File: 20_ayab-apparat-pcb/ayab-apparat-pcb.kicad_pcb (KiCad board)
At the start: 2 copper layers, 105.9 x 43.2 mm, 61 parts, among them K1 CONN_3, K2 CONN_3, P10 CONN_2, P2 CONN_10, P3 CONN_10, P4 CONN_8, P5 CONN_5, P6 CONN_5, P7 CONN_3X2, P8 CONN_4, P9 CONN_2, Q1 MOSFET_P, SW1 SW_PUSH, U1 LM1117, U2 PCF8574, U3 PCF8574, U4 ULN2803, U5 ULN2803, U6 ATMEGA32U4-A, X1 16MHz, X2 USBMINI

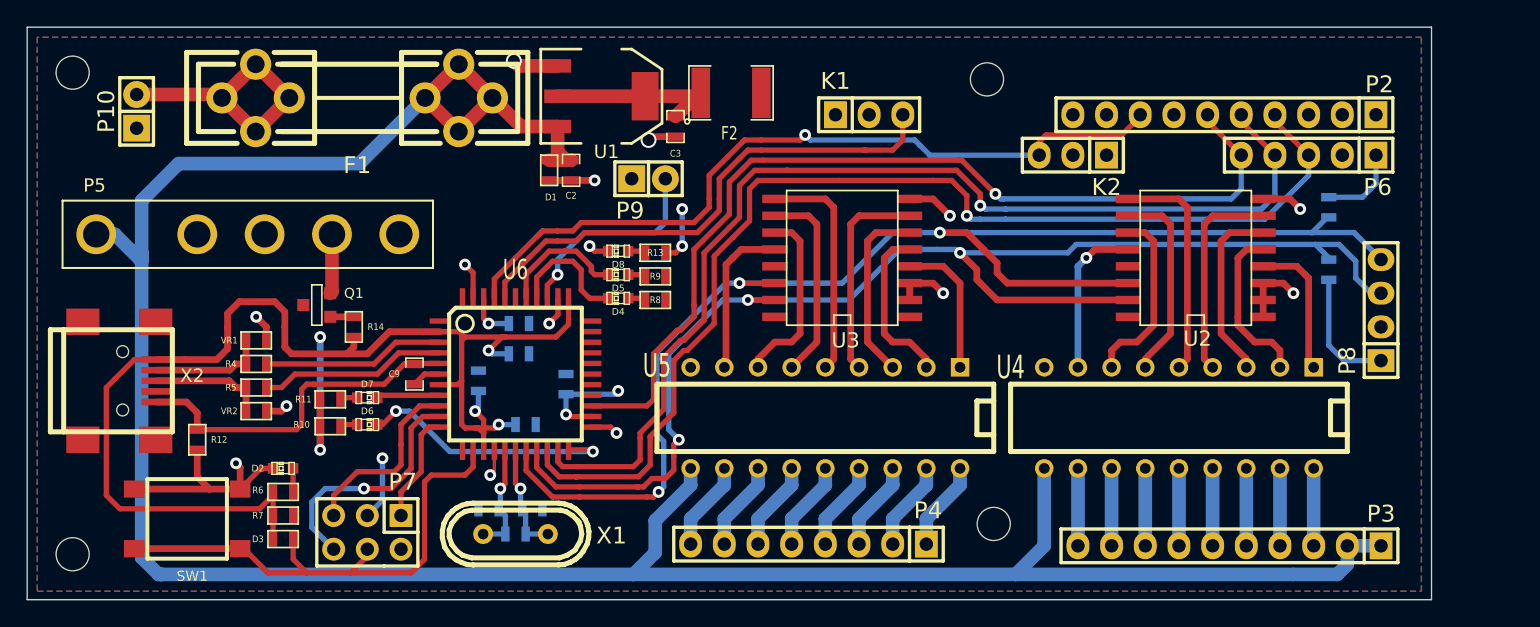
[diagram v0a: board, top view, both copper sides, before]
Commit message: chaned board size
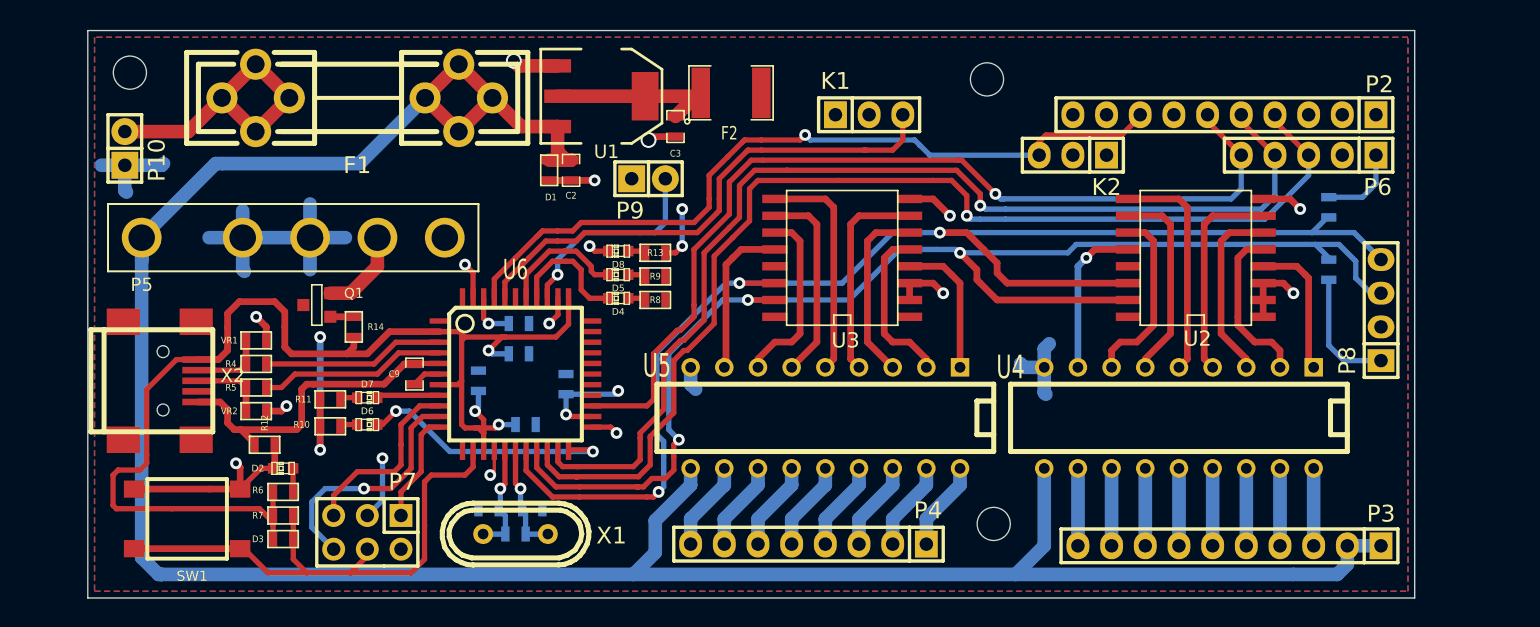
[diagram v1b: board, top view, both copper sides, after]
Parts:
- removed the MH at (62.1, 123.1)
- moved R12 5.09 mm to (76.6, 114.8), turned to 0 degrees
- moved MH 4.32 mm to (66.4, 86.7)
- moved P5 3.44 mm to (67.3, 99.2)
- moved X2 3.05 mm to (68.1, 110.0)
- moved P10 2.93 mm to (66.0, 92.5)
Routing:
- net GND: track 56.0 -> 89.2 mm
- net +12V: track 196.3 -> 188.6 mm
- net /atmega/D-: track 8.68 -> 5.64 mm
- net /atmega/D+: track 8.70 -> 5.65 mm
- net +5V_MACHINE: track 4.50 -> 6.56 mm
- net Net-(F1-Pad2): track 20.9 -> 22.7 mm
- net /atmega/RESET: track 39.6 -> 41.4 mm
- net /atmega/UGND: track 26.6 -> 24.9 mm
- net VUSB: track 94.0 -> 92.9 mm
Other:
- board size 105.9 x 43.2 mm -> 100.1 x 42.8 mm

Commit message: final version (ordered)
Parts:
- moved K1 2.54 mm to (122.2, 87.4)
- moved P2 2.41 mm to (149.0, 87.5)
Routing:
- net /atmega/EOL_L: track 39.0 -> 41.7 mm
- net /atmega/V1: track 81.7 -> 84.1 mm
- net /atmega/BELTSHIFT: track 71.3 -> 73.7 mm
- net /atmega/V2: track 85.4 -> 87.8 mm
- net /atmega/EOL_R: track 58.6 -> 61.1 mm
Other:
- board text added: "ayab-knitting.com"
- board text removed: "thinkstack (c) 2014"
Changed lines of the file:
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@@
     (links 180)
     (no_connects 1)
-    (area 36.46823 73.617524 164.856886 139.0142)
+    (area 40.78623 73.617524 164.856886 133.1341)
     (thickness 1.6)
     (drawings 7)
-    (tracks 708)
+    (tracks 713)
     (zones 0)
     (modules 60)
@@
   )
   (setup
-    (last_trace_width 1.027)
+    (last_trace_width 0.4)
     (user_trace_width 0.4)
     (user_trace_width 0.508)
@@
     (visible_elements FFFFFF7F)
     (pcbplotparams
-      (layerselection 3178497)
+      (layerselection 284196865)
       (usegerberextensions true)
       (excludeedgelayer true)
@@
       (outputformat 1)
       (mirror false)
-      (drillshape 1)
+      (drillshape 0)
       (scaleselection 1)
-      (outputdirectory ""))
+      (outputdirectory out/))
   )
   (net 0 "")
@@
     (tags "LED led 0603 SMD smd SMT smt smdled SMDLED smtled SMTLED")
     (attr smd)
-    (fp_text reference D4 (at 0 -1.016 180) (layer F.SilkS)
+    (fp_text reference D4 (at 0 -0.889 180) (layer F.SilkS)
       (effects (font (size 0.508 0.508) (thickness 0.127)))
     )
@@
     (tags "LED led 0603 SMD smd SMT smt smdled SMDLED smtled SMTLED")
     (attr smd)
-    (fp_text reference D5 (at 0 -1.016 180) (layer F.SilkS)
+    (fp_text reference D5 (at 0 -0.889 180) (layer F.SilkS)
       (effects (font (size 0.508 0.508) (thickness 0.127)))
     )
@@
     (tags "LED led 0603 SMD smd SMT smt smdled SMDLED smtled SMTLED")
     (attr smd)
-    (fp_text reference D8 (at 0 -1.016 180) (layer F.SilkS)
+    (fp_text reference D8 (at 0 -0.889 180) (layer F.SilkS)
       (effects (font (size 0.508 0.508) (thickness 0.127)))
     )
@@
     (descr "Fuseholder, 5x20, open, horizontal, Type-III, universal, inline, lateral,")
     (tags "Fuseholder, 5x20, open, horizontal, Type-III, universal, inline, lateral, Sicherungshalter, offen,")
-    (fp_text reference F1 (at 0 -5.08 180) (layer F.SilkS)
+    (fp_text reference F1 (at -11.684 -4.826 180) (layer F.SilkS)
       (effects (font (thickness 0.3048)))
     )
@@
   )
   (module Pin_Headers:Pin_Header_Straight_1x03 (layer F.Cu)
-    (at 122.174 89.916)
+    (at 122.174 87.376)
     (descr "1 pin")
     (tags "CONN DEV")
@@
   )
   (module Pin_Headers:Pin_Header_Straight_1x10 (layer F.Cu)
-    (at 148.971 89.916 180)
+    (at 148.971 87.503 180)
     (descr "1 pin")
     (tags "CONN DEV")
@@
     (descr "USB Mini-B 5-pin SMD connector")
     (tags "USB, Mini-B, connector")
-    (fp_text reference X2 (at 6.096 -0.381) (layer F.SilkS)
+    (fp_text reference X2 (at 0.254 4.953) (layer F.SilkS)
       (effects (font (size 1.016 1.016) (thickness 0.2032)))
     )
@@
     (pad 1 thru_hole circle (at 0 0) (size 2.49936 2.49936) (drill 2.49936) (layers))
   )
+  (gr_text ayab-knitting.com (at 118.872 90.297) (layer F.SilkS)
+    (effects (font (size 1.5 3) (thickness 0.375)) (justify left))
+  )
   (dimension 100.076 (width 0.3) (layer Dwgs.User)
     (gr_text "100.076 mm" (at 113.284 130.255) (layer Dwgs.User)
@@
   (gr_line (start 163.322 83.566) (end 163.322 126.365) (angle 90) (layer Edge.Cuts) (width 0.1))
   (gr_line (start 63.246 83.566) (end 163.322 83.566) (angle 90) (layer Edge.Cuts) (width 0.1))
-  (gr_text "thinkstack (c) 2014" (at 147.32 86.36) (layer B.Adhes)
-    (effects (font (size 1.5 1.5) (thickness 0.3)) (justify mirror))
-  )
-  (gr_text "AYAB Apparat 2.0" (at 136.398 86.36) (layer F.Adhes)
+  (gr_text "AYAB Apparat 2.0" (at 71.501 94.615) (layer F.SilkS)
     (effects (font (size 1.5 1.5) (thickness 0.3)) (justify left))
   )
@@
   (segment (start 100.711 98.806) (end 106.045 98.806) (width 0.4) (layer B.Cu) (net 5))
   (segment (start 98.679 100.838) (end 100.711 98.806) (width 0.4) (layer B.Cu) (net 5))
+  (segment (start 147.701 87.503) (end 147.701 89.916) (width 0.4) (layer F.Cu) (net 6))
+  (segment (start 147.701 90.424) (end 150.241 92.964) (width 0.4) (layer F.Cu) (net 6))
   (segment (start 147.701 89.916) (end 147.701 90.424) (width 0.4) (layer F.Cu) (net 6))
-  (segment (start 147.701 90.424) (end 150.241 92.964) (width 0.4) (layer F.Cu) (net 6))
   (segment (start 132.334 96.266) (end 149.479 96.266) (width 0.4) (layer B.Cu) (net 6))
   (segment (start 129.159 93.345) (end 131.699 95.885) (width 0.4) (layer F.Cu) (net 6))
@@
   (segment (start 74.7141 109.1819) (end 75.184 108.712) (width 0.4) (layer F.Cu) (net 8))
   (segment (start 75.184 108.712) (end 75.184 106.934) (width 0.508) (layer F.Cu) (net 8))
-  (segment (start 121.92 92.583) (end 123.952 92.583) (width 0.4) (layer F.Cu) (net 9))
+  (segment (start 124.714 87.376) (end 124.714 90.043) (width 0.4) (layer F.Cu) (net 9))
+  (segment (start 123.952 92.583) (end 124.714 91.821) (width 0.4) (layer F.Cu) (net 9))
   (segment (start 124.714 91.821) (end 124.714 90.043) (width 0.4) (layer F.Cu) (net 9))
-  (segment (start 123.952 92.583) (end 124.714 91.821) (width 0.4) (layer F.Cu) (net 9))
+  (segment (start 123.952 92.583) (end 121.92 92.583) (width 0.4) (layer F.Cu) (net 9))
   (segment (start 114.046 92.583) (end 121.92 92.583) (width 0.4) (layer F.Cu) (net 9))
   (segment (start 112.903 92.71) (end 113.03 92.583) (width 0.4) (layer F.Cu) (net 9))
@@
   (segment (start 112.395 93.218) (end 112.903 92.71) (width 0.4) (layer F.Cu) (net 9))
   (segment (start 121.92 92.583) (end 121.793 92.583) (width 0.4) (layer F.Cu) (net 9))
+  (segment (start 142.621 87.503) (end 142.621 89.916) (width 0.4) (layer F.Cu) (net 10))
+  (segment (start 135.001 91.948) (end 135.001 92.964) (width 0.4) (layer F.Cu) (net 10))
+  (segment (start 135.509 91.44) (end 135.001 91.948) (width 0.4) (layer F.Cu) (net 10))
+  (segment (start 141.224 91.44) (end 135.509 91.44) (width 0.4) (layer F.Cu) (net 10))
+  (segment (start 142.621 90.043) (end 141.224 91.44) (width 0.4) (layer F.Cu) (net 10))
+  (segment (start 142.621 89.916) (end 142.621 90.043) (width 0.4) (layer F.Cu) (net 10))
   (segment (start 125.984 92.202) (end 126.746 92.964) (width 0.4) (layer B.Cu) (net 10))
   (segment (start 116.967 91.821) (end 117.348 91.44) (width 0.4) (layer F.Cu) (net 10))
@@
   (segment (start 114.046 91.821) (end 116.967 91.821) (width 0.4) (layer F.Cu) (net 10))
   (segment (start 126.746 92.964) (end 135.001 92.964) (width 0.4) (layer B.Cu) (net 10))
-  (segment (start 142.621 89.916) (end 142.621 90.043) (width 0.4) (layer F.Cu) (net 10))
-  (segment (start 142.621 90.043) (end 141.224 91.44) (width 0.4) (layer F.Cu) (net 10))
-  (segment (start 141.224 91.44) (end 135.509 91.44) (width 0.4) (layer F.Cu) (net 10))
-  (segment (start 135.509 91.44) (end 135.001 91.948) (width 0.4) (layer F.Cu) (net 10))
-  (segment (start 135.001 91.948) (end 135.001 92.964) (width 0.4) (layer F.Cu) (net 10))
   (segment (start 108.712 98.044) (end 108.712 98.044) (width 0.4) (layer F.Cu) (net 10))
   (segment (start 104.902 98.044) (end 108.712 98.044) (width 0.4) (layer F.Cu) (net 10))
@@
   (segment (start 89.789 108.6739) (end 87.9221 108.6739) (width 0.4) (layer F.Cu) (net 26))
   (segment (start 87.9221 108.6739) (end 87.884 108.712) (width 0.4) (layer F.Cu) (net 26))
+  (segment (start 150.241 87.503) (end 150.241 89.916) (width 0.4) (layer F.Cu) (net 27))
+  (segment (start 150.241 90.424) (end 152.781 92.964) (width 0.4) (layer F.Cu) (net 27))
   (segment (start 150.241 89.916) (end 150.241 90.424) (width 0.4) (layer F.Cu) (net 27))
-  (segment (start 150.241 90.424) (end 152.781 92.964) (width 0.4) (layer F.Cu) (net 27))
   (segment (start 132.461 97.028) (end 151.765 97.028) (width 0.4) (layer B.Cu) (net 27))
   (segment (start 130.683 96.774) (end 130.937 97.028) (width 0.4) (layer B.Cu) (net 27))
@@
   (segment (start 112.395 95.25) (end 112.395 95.631) (width 0.4) (layer F.Cu) (net 27))
   (segment (start 112.395 95.631) (end 112.395 97.663) (width 0.4) (layer F.Cu) (net 27))
+  (segment (start 152.781 87.503) (end 152.781 89.916) (width 0.4) (layer F.Cu) (net 28))
+  (segment (start 152.781 90.424) (end 155.321 92.964) (width 0.4) (layer F.Cu) (net 28))
   (segment (start 152.781 89.916) (end 152.781 90.424) (width 0.4) (layer F.Cu) (net 28))
-  (segment (start 152.781 90.424) (end 155.321 92.964) (width 0.4) (layer F.Cu) (net 28))
   (segment (start 132.461 97.79) (end 152.019 97.79) (width 0.4) (layer B.Cu) (net 28))
   (segment (start 127 94.869) (end 128.397 94.869) (width 0.4) (layer F.Cu) (net 28))
